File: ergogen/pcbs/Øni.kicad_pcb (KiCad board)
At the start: 2 copper layers, 112.5 x 99.9 mm, 37 parts

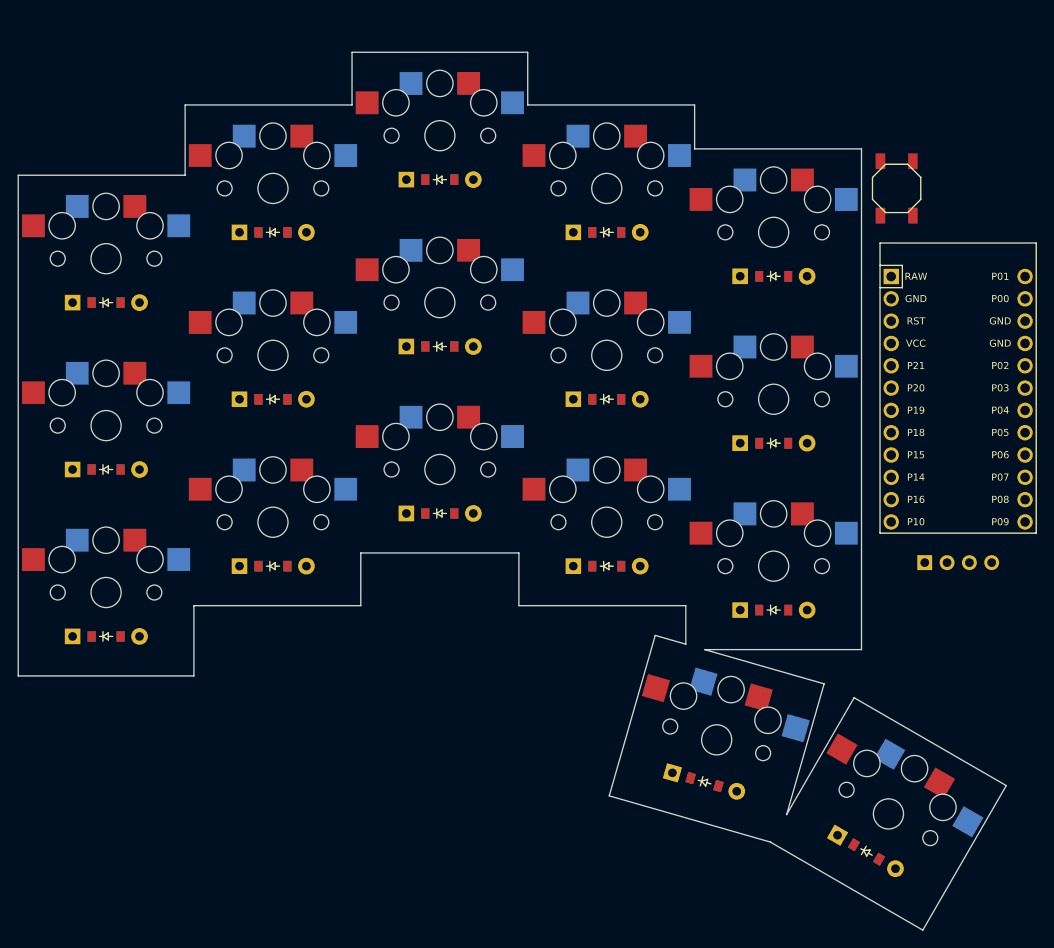
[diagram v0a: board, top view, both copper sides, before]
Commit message: 3 thumb keys
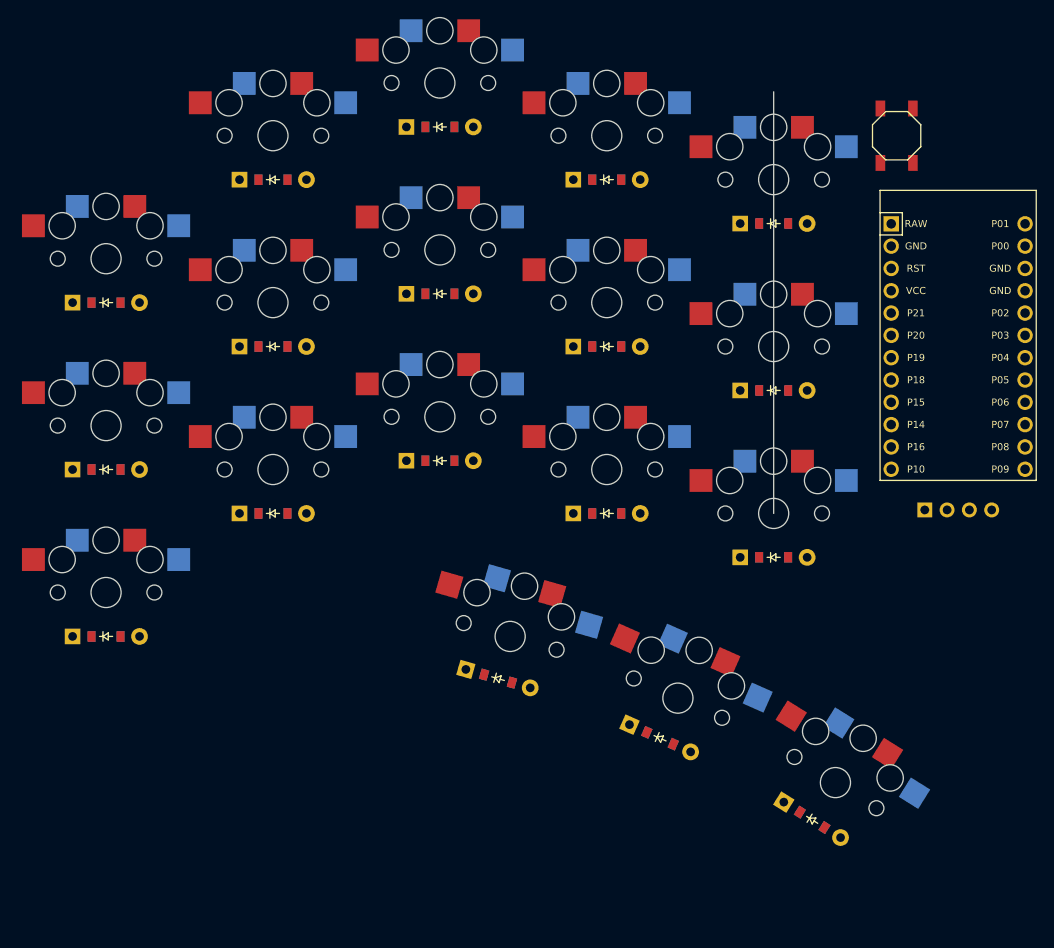
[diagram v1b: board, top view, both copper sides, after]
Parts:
- added D18: , ComboDiode, F.Cu at (210.4, 175.9)
- added S18: , PG1350, F.Cu at (213.0, 171.6)
- moved S17 27.4 mm to (195.1, 162.0), turned to -24 degrees
- moved D17 26.8 mm to (193.1, 166.6), turned to -24 degrees
- moved D16 26.3 mm to (174.6, 159.8)
- moved S16 26.3 mm to (176.0, 155.0)
- moved B1 6.00 mm to (220.0, 98.0)
- moved D10 6.00 mm to (187.0, 141.0)
- moved D11 6.00 mm to (187.0, 122.0)
- moved D12 6.00 mm to (187.0, 103.0)
- moved D13 6.00 mm to (206.0, 146.0)
- moved D14 6.00 mm to (206.0, 127.0)
- moved D15 6.00 mm to (206.0, 108.0)
- moved D4 6.00 mm to (149.0, 141.0)
- moved D5 6.00 mm to (149.0, 122.0)
- moved D6 6.00 mm to (149.0, 103.0)
- moved D7 6.00 mm to (168.0, 135.0)
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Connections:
- net home_thumb renamed home_default
- net near_thumb renamed near_default
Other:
- board outline removed
